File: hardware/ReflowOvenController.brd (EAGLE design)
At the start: 91.4 x 53.3 mm, 27 parts, among them U1 VSK-S5, U2 MAX31856, U3 LTV-354T, U4 FODM3053, U5 T25

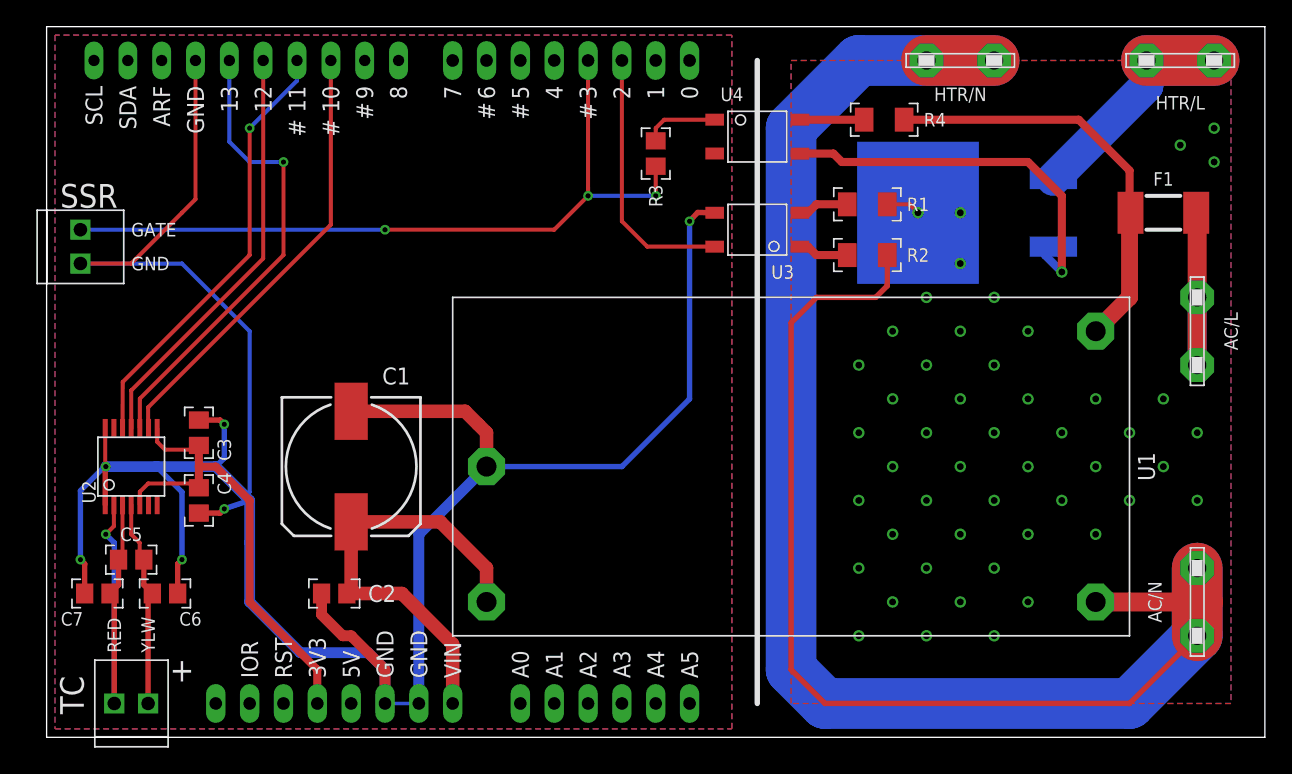
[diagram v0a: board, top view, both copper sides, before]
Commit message: Improved mechanical layout. Added status leds.
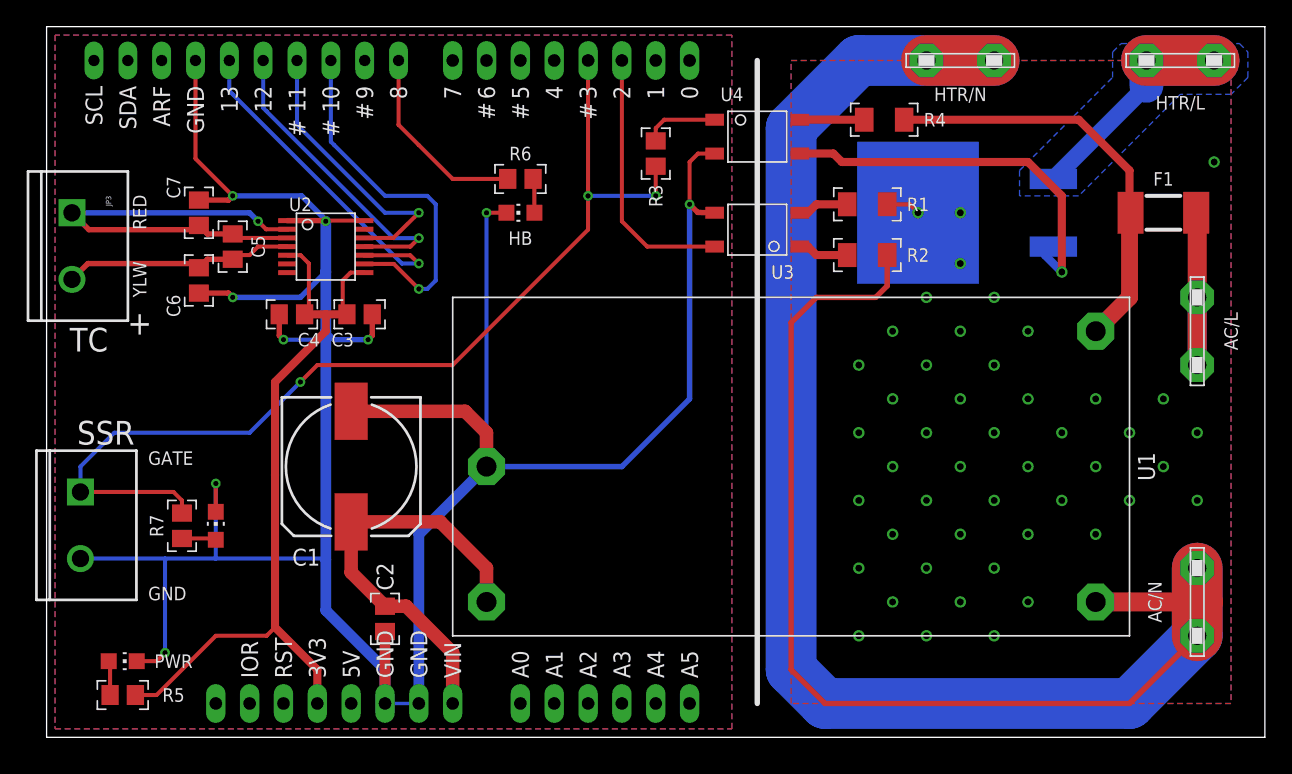
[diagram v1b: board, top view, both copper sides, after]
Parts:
- added LED1, LED2, LED3: (no value), SmslsTron:CHIP-LED0805
- added R5, R6, R7: 390, SmslsTron:R0805
- added U$1: SILK_QC, SmslsTron:SILK_QC
- JP1, JP3: value M022.54MM_SCREWTERM -> M025MM; device ReflowOvenController:1X02_2.54_SCREWTERM -> SmslsTron:SCREWTERMINAL-5MM-2
- moved JP3 37.3 mm to (1.91, 39.4), turned to 270 degrees
- moved C7 29.6 mm to (11.4, 39.4), turned to 90 degrees
- moved C5 24.7 mm to (14.0, 36.8), turned to 270 degrees
- moved C6 23.6 mm to (11.4, 34.3), turned to 270 degrees
- moved U2 22.0 mm to (21.0, 36.8), turned to 270 degrees
- moved JP1 17.1 mm to (2.54, 18.4), turned to 270 degrees
- moved C4 15.6 mm to (18.4, 31.8), turned to 180 degrees
- moved C3 15.0 mm to (23.5, 31.8), turned to 0 degrees
- moved C2 4.26 mm to (25.4, 8.89), turned to 270 degrees
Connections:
- net D0 renamed RXD/D0
- net D1 renamed TXD/D1
- removed net D8: DIO-H.10
- new net HB/D8: DIO-H.10, R6.1
- new net N$6: LED3.A, R7.2
- new net N$7: LED1.A, R5.2
- new net N$9: LED2.A, R6.2
- net +3V3: now also R5.1
- net GND: now also JP1.2, LED1.C, LED2.C, LED3.C; no longer JP1.P2
- net HTR_SIG/D3: now also JP1.1, R7.1; no longer JP1.P1
- net TC+: now also JP3.2; no longer JP3.P2
- net TC-: now also JP3.1; no longer JP3.P1
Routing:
- net GND: track 198.2 -> 223.9 mm, vias 6 -> 9
- net +3V3: track 35.7 -> 58.2 mm
- net HTR_SIG/D3: track 57.3 -> 76.8 mm
- net HB/D8: track 0.00 -> 14.7 mm
- net MOSI/D11: track 33.0 -> 21.6 mm
- net SCLK/D13: track 35.2 -> 26.2 mm
- net MISO/D12: track 31.7 -> 23.7 mm, vias 0 -> 1
- net TC_CS/D10: track 33.3 -> 28.1 mm, vias 0 -> 1
- net TC-: track 30.8 -> 33.9 mm
- net N$9: track 0.00 -> 2.58 mm
- net N$7: track 0.00 -> 2.58 mm
- net N$6: track 0.00 -> 2.58 mm
- net TC+: track 15.7 -> 17.5 mm
- net VIN: track 33.6 -> 31.9 mm
- net AC/L: vias 49 -> 47
- added copper zone on layer 16, net HTR/L
